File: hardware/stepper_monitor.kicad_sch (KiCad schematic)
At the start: 59 parts, among them J1 Conn_01x04_Male, J2 Conn_01x04_Male, J3 Conn_01x02_Male, J4 USB_C_Receptacle_USB2.0, M1 Motor-simple_stepper_motor_an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, Q1 MMDT2222A, SW1 SW_Push, U1 5V, U2 CP2102N-A01-GQFN28, U3 AMS1117-3.3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

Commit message: Generated JLCPCB produciton files.
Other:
- note added: "CXXXXX ids are JLCPCB/LCSC part numbers."
- note added: "Default"
- note added: "Solder a LCSC C2935458 connector for JTAG debugger."
- note removed: "JTAG Connector"
- note removed: "Solder LCSC C2935458 For JTAG Debugging"
- moved on the sheet: R17, R18
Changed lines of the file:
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@@
     (stroke (width 0) (type default) (color 0 0 0 0))
   )
-  (wire (pts (xy 148.59 114.935) (xy 152.4 114.935))
+  (wire (pts (xy 149.225 112.395) (xy 153.035 112.395))
     (stroke (width 0) (type default) (color 0 0 0 0))
   )
@@
     (stroke (width 0) (type default) (color 0 0 0 0))
   )
-  (wire (pts (xy 160.02 105.41) (xy 160.02 106.68))
+  (wire (pts (xy 160.655 102.87) (xy 160.655 104.14))
     (stroke (width 0) (type default) (color 0 0 0 0))
   )
@@
     (stroke (width 0) (type default) (color 0 0 0 0))
   )
-  (wire (pts (xy 157.48 114.935) (xy 160.02 114.935))
+  (wire (pts (xy 158.115 112.395) (xy 160.655 112.395))
     (stroke (width 0) (type default) (color 0 0 0 0))
   )
@@
     (stroke (width 0) (type default) (color 0 0 0 0))
   )
-  (wire (pts (xy 160.02 114.935) (xy 160.02 116.205))
+  (wire (pts (xy 160.655 112.395) (xy 160.655 113.665))
     (stroke (width 0) (type default) (color 0 0 0 0))
   )
@@
     (stroke (width 0) (type default) (color 0 0 0 0))
   )
-  (wire (pts (xy 148.59 105.41) (xy 152.4 105.41))
+  (wire (pts (xy 149.225 102.87) (xy 153.035 102.87))
     (stroke (width 0) (type default) (color 0 0 0 0))
   )
@@
     (stroke (width 0) (type default) (color 0 0 0 0))
   )
-  (wire (pts (xy 157.48 105.41) (xy 160.02 105.41))
+  (wire (pts (xy 158.115 102.87) (xy 160.655 102.87))
     (stroke (width 0) (type default) (color 0 0 0 0))
   )
@@
     (stroke (width 0) (type default) (color 0 0 0 0))
   )
-  (text "Solder LCSC C2935458\nFor JTAG Debugging" (at 148.59 186.69 0)
+  (text "Solder a LCSC C2935458\nconnector for JTAG debugger."
+    (at 141.605 191.135 0)
     (effects (font (size 1.27 1.27)) (justify left bottom))
   )
@@
     (effects (font (size 1.27 1.27)) (justify left bottom))
   )
-  (text "JTAG Connector" (at 163.195 191.135 180)
-    (effects (font (size 1.27 1.27)) (justify right bottom))
-  )
   (text "Reserved 2" (at 140.97 141.605 0)
     (effects (font (size 1.27 1.27)) (justify left bottom))
@@
     (effects (font (size 1.27 1.27)) (justify left bottom))
   )
+  (text "CXXXXX ids are JLCPCB/LCSC part numbers." (at 184.15 178.435 0)
+    (effects (font (size 1.27 1.27)) (justify left bottom))
+  )
   (text "Reserved 1" (at 140.97 138.43 0)
     (effects (font (size 1.27 1.27)) (justify left bottom))
@@
     (effects (font (size 1.27 1.27)) (justify right bottom))
   )
+  (text "Default" (at 168.91 132.08 0)
+    (effects (font (size 1.27 1.27)) (justify left bottom))
+  )
   (text "R17" (at 163.195 128.905 0)
     (effects (font (size 1.27 1.27)) (justify left bottom))
@@
     (effects (font (size 1.27 1.27)) (justify right bottom))
   )
-  (text "ESP32 Stepper Motor Analyzer 1.4.1" (at 183.515 175.26 0)
+  (text "ESP32 Stepper Motor Analyzer 1.4.1" (at 184.15 173.355 0)
     (effects (font (size 2 2)) (justify left bottom))
   )
@@
     )
   )
-  (global_label "CFG2" (shape passive) (at 148.59 114.935 180) (fields_autoplaced)
+  (global_label "CFG2" (shape passive) (at 149.225 112.395 180) (fields_autoplaced)
     (effects (font (size 1.27 1.27)) (justify right))
-    (property "Intersheet References" "${INTERSHEET_REFS}" (id 0) (at 141.4277 114.8556 0)
+    (property "Intersheet References" "${INTERSHEET_REFS}" (id 0) (at 142.0627 112.3156 0)
       (effects (font (size 1.27 1.27)) (justify right) hide)
     )
@@
     )
   )
-  (global_label "CFG1" (shape passive) (at 148.59 105.41 180) (fields_autoplaced)
+  (global_label "CFG1" (shape passive) (at 149.225 102.87 180) (fields_autoplaced)
     (effects (font (size 1.27 1.27)) (justify right))
-    (property "Intersheet References" "${INTERSHEET_REFS}" (id 0) (at 141.4277 105.3306 0)
+    (property "Intersheet References" "${INTERSHEET_REFS}" (id 0) (at 142.0627 102.7906 0)
       (effects (font (size 1.27 1.27)) (justify right) hide)
     )
@@
     (pin "1")
   )
-  (symbol (lib_id "Device:R_Small_US") (at 154.94 114.935 90) (unit 1)
-    (in_bom yes) (on_board yes)
-    (property "Reference" "R18" (id 0) (at 153.035 112.395 90))
-    (property "Value" "DNP" (id 1) (at 157.48 112.395 90))
-    (property "Footprint" "Resistor_SMD:R_0402_1005Metric" (id 2) (at 154.94 114.935 0)
-      (effects (font (size 1.27 1.27)) hide)
-    )
-    (property "Datasheet" "~" (id 3) (at 154.94 114.935 0)
-      (effects (font (size 1.27 1.27)) hide)
-    )
-    (property "LCSC" "DNP" (id 4) (at 162.56 112.395 90))
+  (symbol (lib_id "Device:R_Small_US") (at 155.575 112.395 90) (unit 1)
+    (in_bom yes) (on_board yes)
+    (property "Reference" "R18" (id 0) (at 153.67 109.855 90))
+    (property "Value" "DNP" (id 1) (at 158.115 109.855 90))
+    (property "Footprint" "Resistor_SMD:R_0402_1005Metric" (id 2) (at 155.575 112.395 0)
+      (effects (font (size 1.27 1.27)) hide)
+    )
+    (property "Datasheet" "~" (id 3) (at 155.575 112.395 0)
+      (effects (font (size 1.27 1.27)) hide)
+    )
+    (property "LCSC" "DNP" (id 4) (at 163.195 109.855 90))
     (pin "1")
     (pin "2")
@@
     (pin "3")
   )
-  (symbol (lib_id "power:GNDD") (at 160.02 116.205 0) (unit 1)
-    (in_bom yes) (on_board yes)
-    (property "Reference" "#PWR022" (id 0) (at 160.02 122.555 0)
-      (effects (font (size 1.27 1.27)) hide)
-    )
-    (property "Value" "GNDD" (id 1) (at 160.1216 120.142 0)
-      (effects (font (size 1.27 1.27)) hide)
-    )
-    (property "Footprint" "" (id 2) (at 160.02 116.205 0)
-      (effects (font (size 1.27 1.27)) hide)
-    )
-    (property "Datasheet" "" (id 3) (at 160.02 116.205 0)
+  (symbol (lib_id "power:GNDD") (at 160.655 113.665 0) (unit 1)
+    (in_bom yes) (on_board yes)
+    (property "Reference" "#PWR022" (id 0) (at 160.655 120.015 0)
+      (effects (font (size 1.27 1.27)) hide)
+    )
+    (property "Value" "GNDD" (id 1) (at 160.7566 117.602 0)
+      (effects (font (size 1.27 1.27)) hide)
+    )
+    (property "Footprint" "" (id 2) (at 160.655 113.665 0)
+      (effects (font (size 1.27 1.27)) hide)
+    )
+    (property "Datasheet" "" (id 3) (at 160.655 113.665 0)
       (effects (font (size 1.27 1.27)) hide)
     )
@@
     (pin "2")
   )
-  (symbol (lib_id "power:GNDD") (at 160.02 106.68 0) (unit 1)
-    (in_bom yes) (on_board yes)
-    (property "Reference" "#PWR021" (id 0) (at 160.02 113.03 0)
-      (effects (font (size 1.27 1.27)) hide)
-    )
-    (property "Value" "GNDD" (id 1) (at 160.1216 110.617 0)
-      (effects (font (size 1.27 1.27)) hide)
-    )
-    (property "Footprint" "" (id 2) (at 160.02 106.68 0)
-      (effects (font (size 1.27 1.27)) hide)
-    )
-    (property "Datasheet" "" (id 3) (at 160.02 106.68 0)
+  (symbol (lib_id "power:GNDD") (at 160.655 104.14 0) (unit 1)
+    (in_bom yes) (on_board yes)
+    (property "Reference" "#PWR021" (id 0) (at 160.655 110.49 0)
+      (effects (font (size 1.27 1.27)) hide)
+    )
+    (property "Value" "GNDD" (id 1) (at 160.7566 108.077 0)
+      (effects (font (size 1.27 1.27)) hide)
+    )
+    (property "Footprint" "" (id 2) (at 160.655 104.14 0)
+      (effects (font (size 1.27 1.27)) hide)
+    )
+    (property "Datasheet" "" (id 3) (at 160.655 104.14 0)
       (effects (font (size 1.27 1.27)) hide)
     )
@@
       (effects (font (size 1.27 1.27)) hide)
     )
-    (property "LCSC" "C720477" (id 4) (at 73.025 179.705 90))
+    (property "LCSC" "C720477" (id 4) (at 66.675 186.69 90))
     (pin "1")
     (pin "2")
@@
     (pin "1")
   )
-  (symbol (lib_id "Device:R_Small_US") (at 154.94 105.41 90) (unit 1)
-    (in_bom yes) (on_board yes)
-    (property "Reference" "R17" (id 0) (at 153.035 102.87 90))
-    (property "Value" "DNP" (id 1) (at 157.48 102.87 90))
-    (property "Footprint" "Resistor_SMD:R_0402_1005Metric" (id 2) (at 154.94 105.41 0)
-      (effects (font (size 1.27 1.27)) hide)
-    )
-    (property "Datasheet" "~" (id 3) (at 154.94 105.41 0)
-      (effects (font (size 1.27 1.27)) hide)
-    )
-    (property "LCSC" "DNP" (id 4) (at 162.56 102.87 90))
-    (pin "1")
-    (pin "2")
+  (symbol (lib_id "Device:R_Small_US") (at 155.575 102.87 90) (unit 1)
+    (in_bom yes) (on_board yes)
+    (property "Reference" "R17" (id 0) (at 153.67 100.33 90))
+    (property "Value" "DNP" (id 1) (at 158.115 100.33 90))
+    (property "Footprint" "Resistor_SMD:R_0402_1005Metric" (id 2) (at 155.575 102.87 0)
+      (effects (font (size 1.27 1.27)) hide)
+    )
+    (property "Datasheet" "~" (id 3) (at 155.575 102.87 0)
+      (effects (font (size 1.27 1.27)) hide)
+    )
+    (property "LCSC" "DNP" (id 4) (at 163.195 100.33 90))
+    (pin "1")
+    (pin "2")

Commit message: Changed LCSC part number of green LED
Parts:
- D2: LCSC C165978 -> C130722
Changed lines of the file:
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@@
       (effects (font (size 1.27 1.27)) hide)
     )
-    (property "LCSC" "C165978" (id 4) (at 36.195 186.69 90)
+    (property "LCSC" "C130722" (id 4) (at 36.195 186.69 90)
       (effects (font (size 1.27 1.27)) (justify right))
     )

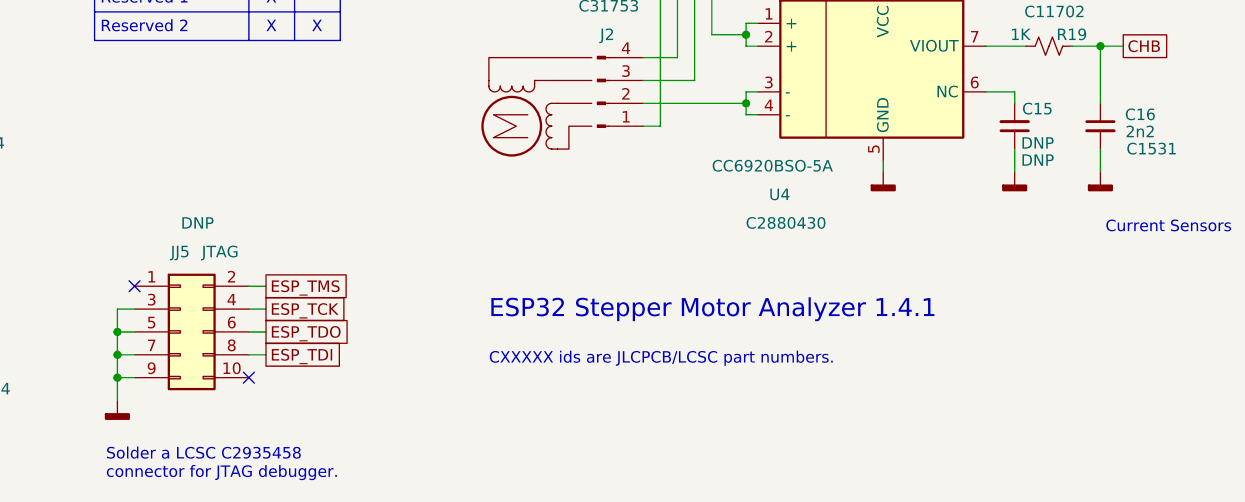
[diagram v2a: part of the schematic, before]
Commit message: Renamed jj5 to j5. Increased version to 1.4.2. This is one commit past order of 1.4.1 from JLCPCB.
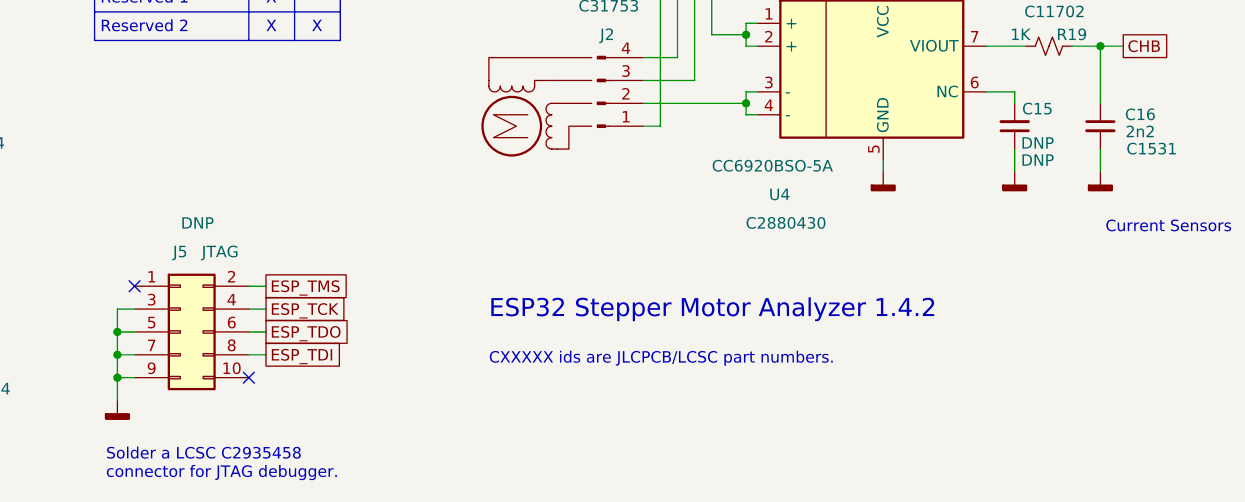
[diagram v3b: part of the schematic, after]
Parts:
- renumbered JJ5 to J5
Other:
- note added: "ESP32 Stepper Motor Analyzer 1.4.2"
- note removed: "ESP32 Stepper Motor Analyzer 1.4.1"
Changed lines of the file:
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@@
     (effects (font (size 1.27 1.27)) (justify right bottom))
   )
-  (text "ESP32 Stepper Motor Analyzer 1.4.1" (at 184.15 173.355 0)
+  (text "ESP32 Stepper Motor Analyzer 1.4.2" (at 184.15 173.355 0)
     (effects (font (size 2 2)) (justify left bottom))
   )
@@
   (symbol (lib_id "Connector_Generic:Conn_02x05_Odd_Even") (at 149.86 174.625 0) (unit 1)
     (in_bom yes) (on_board yes)
-    (property "Reference" "JJ5" (id 0) (at 149.86 165.735 0))
+    (property "Reference" "J5" (id 0) (at 149.86 165.735 0))
     (property "Value" "JTAG" (id 1) (at 154.305 165.735 0))
     (property "Footprint" "stepper_monitor:PinHeader_2x05_P1.27mm_Vertical_SMD" (id 2) (at 149.86 174.625 0)
@@
     )
     (path "/4aa030a1-7b9f-40c4-b8f1-bb12c1377f35"
-      (reference "JJ5") (unit 1) (value "JTAG") (footprint "stepper_monitor:PinHeader_2x05_P1.27mm_Vertical_SMD")
+      (reference "J5") (unit 1) (value "JTAG") (footprint "stepper_monitor:PinHeader_2x05_P1.27mm_Vertical_SMD")
     )
     (path "/64c584ec-f1bc-453f-8b60-7c99d996b567"

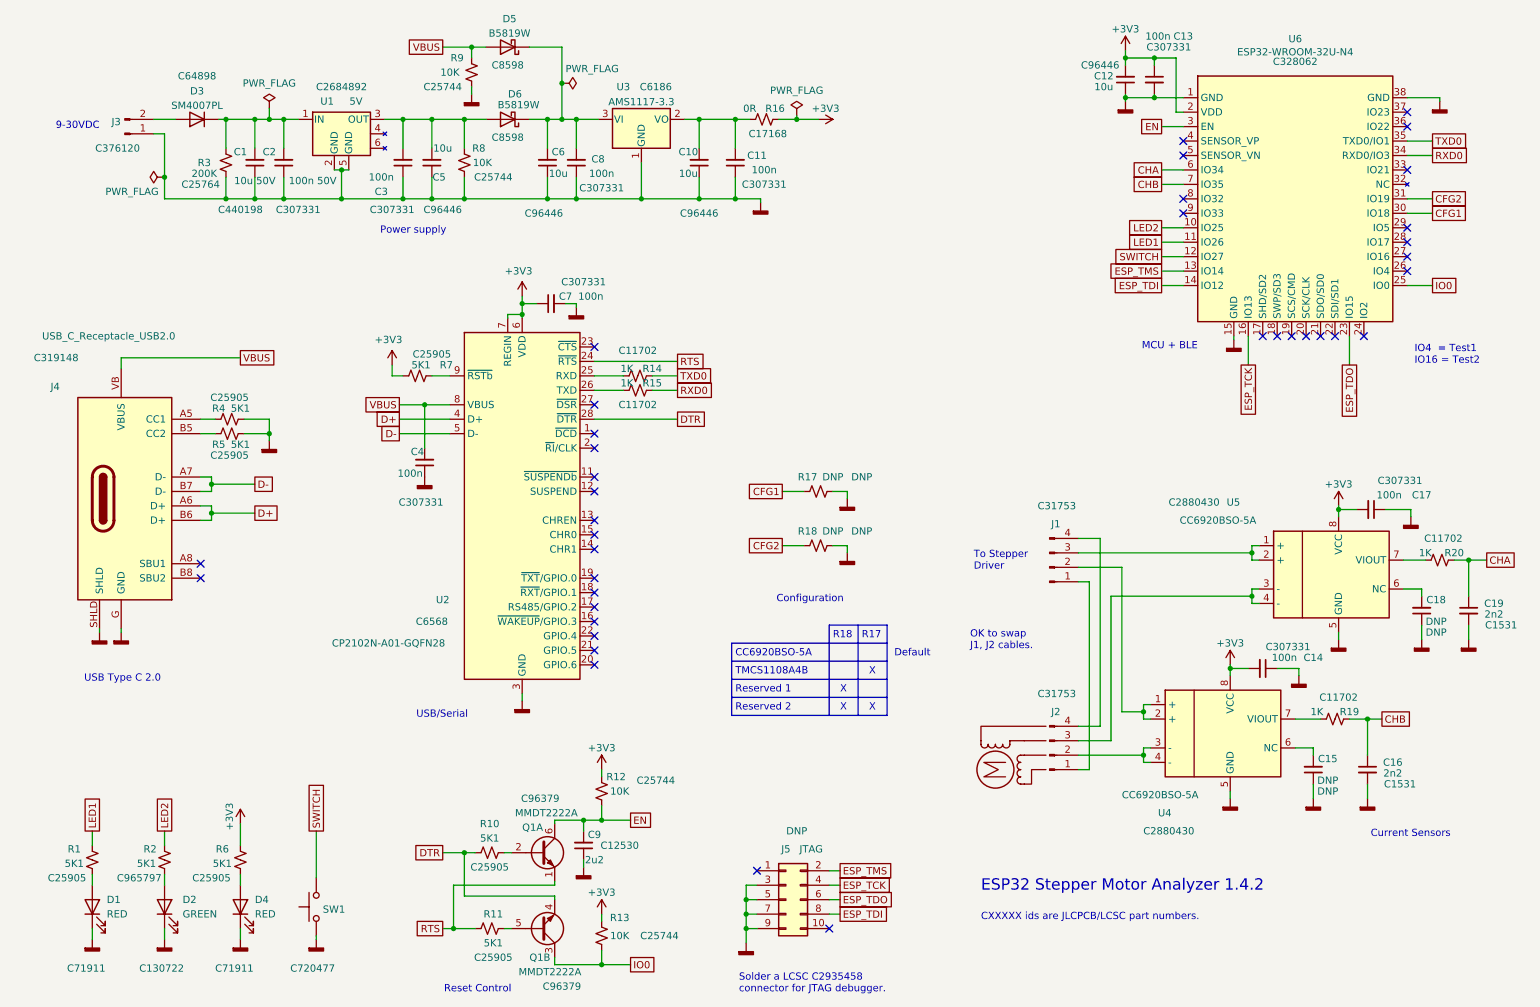
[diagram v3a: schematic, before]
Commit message: Upgraded kicad to 7.0 (design version incremented to 1.4.2)
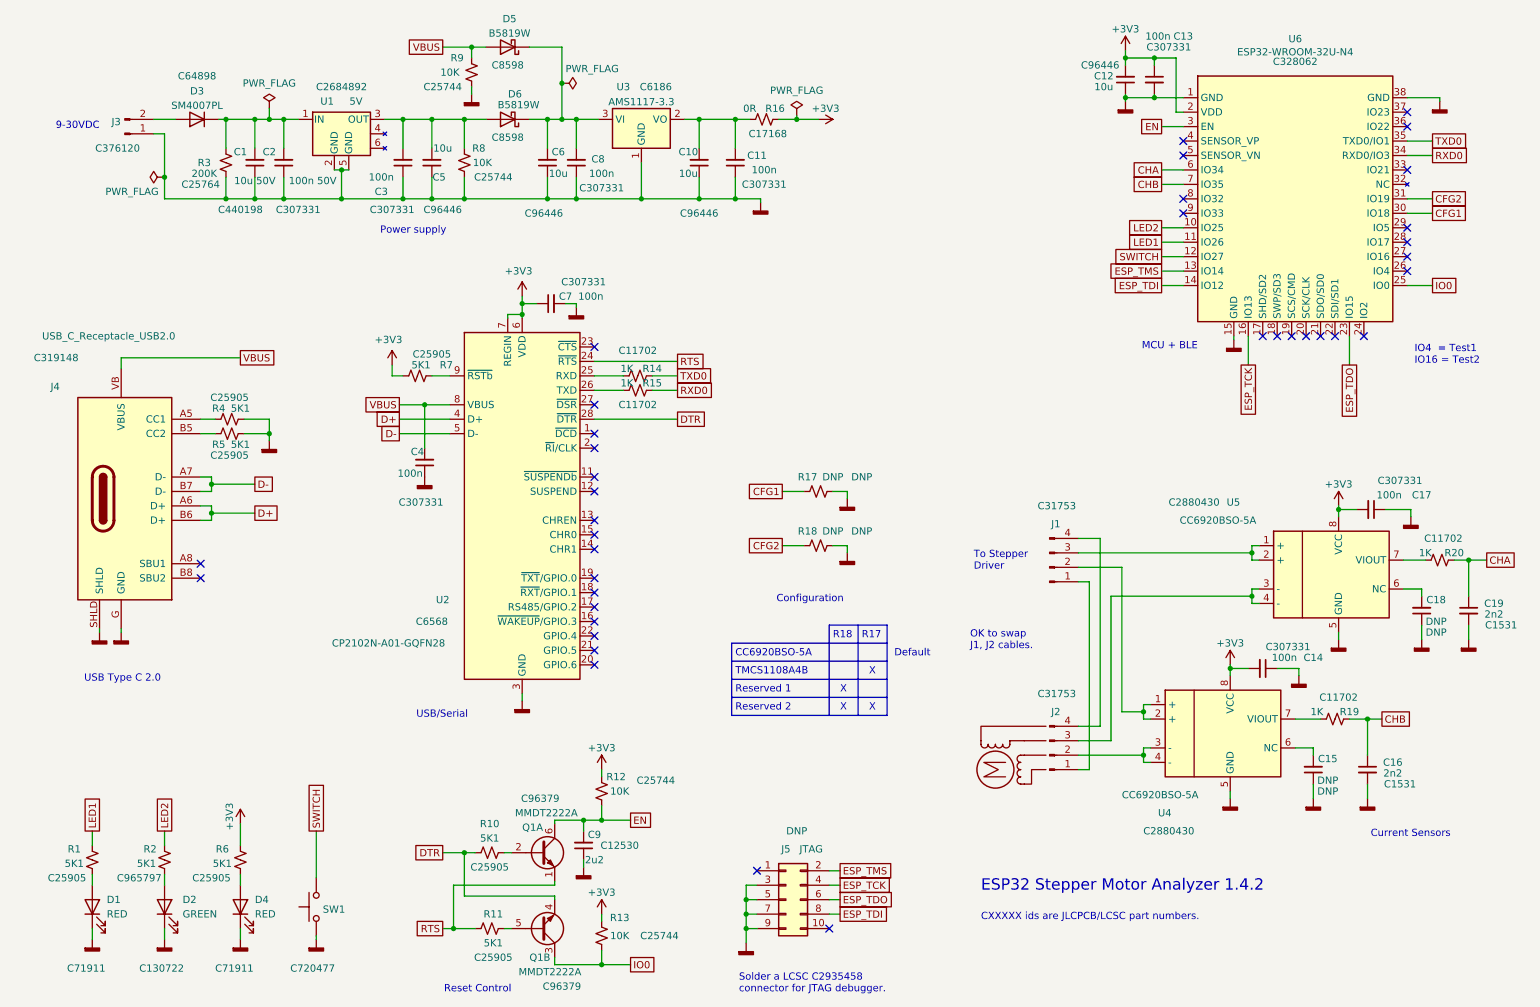
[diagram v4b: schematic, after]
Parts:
- J1, J2: value Conn_01x04_Male -> Conn_01x04_Pin; symbol Connector:Conn_01x04_Male -> Connector:Conn_01x04_Pin
- J3: value Conn_01x02_Male -> Conn_01x02_Pin; symbol Connector:Conn_01x02_Male -> Connector:Conn_01x02_Pin
